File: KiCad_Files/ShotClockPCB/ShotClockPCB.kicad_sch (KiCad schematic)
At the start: 0 parts

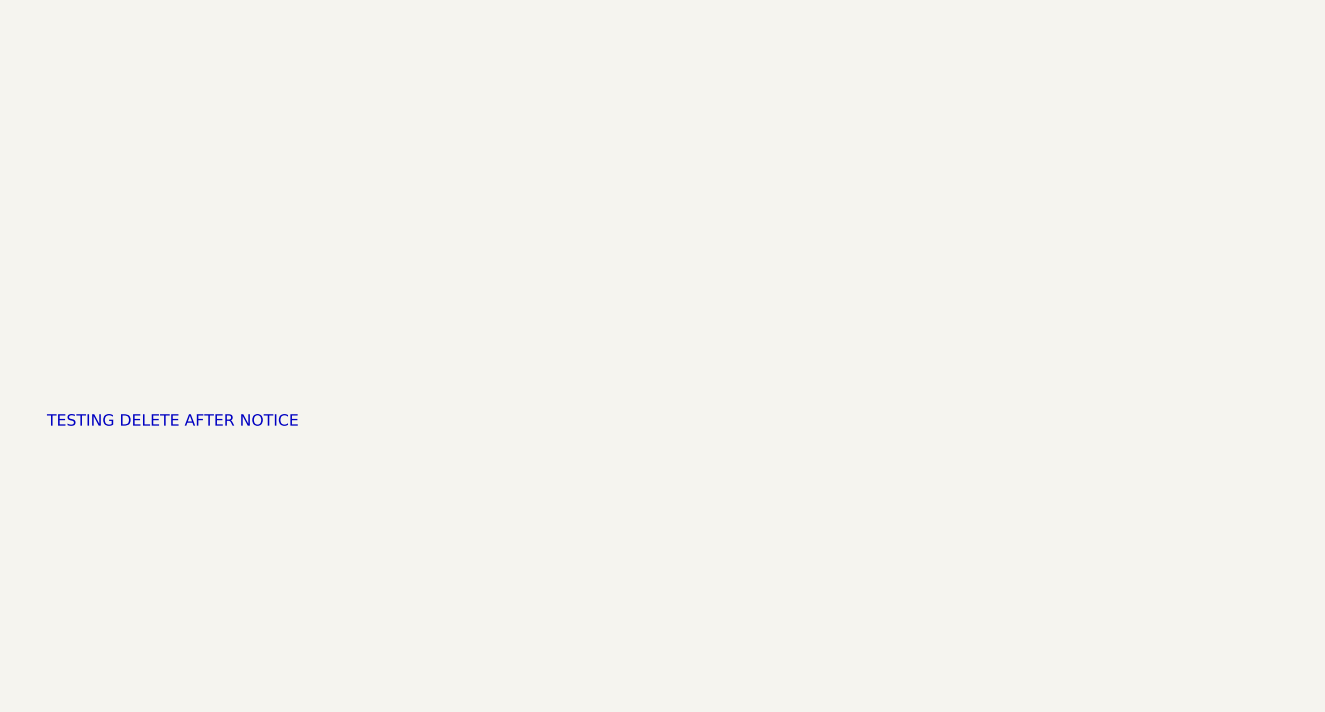
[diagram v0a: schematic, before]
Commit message: Added KiCad Schem and KiCad footprint libraries
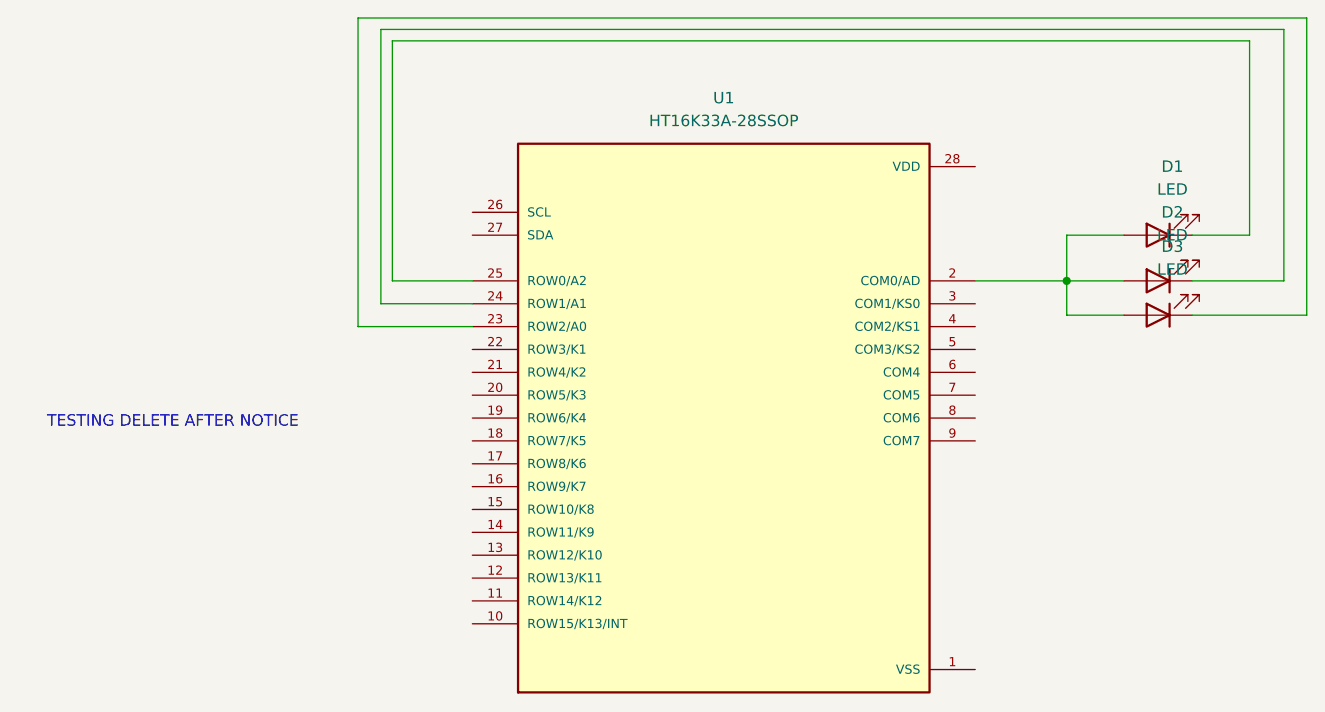
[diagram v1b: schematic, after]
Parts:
- added D1, D2, D3: LED, symbol Device:LED
- added U1: HT16K33A-28SSOP, HT16K33A-28SSOP:SOP63P600X175-28N, symbol HT16K33A-28SSOP:HT16K33A-28SSOP
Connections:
- new net: D1.2 (A), D2.2 (A), D3.2 (A), U1.2 (COM0/AD)
- new net: D3.1 (K), U1.23 (ROW2/A0)
- new net: D2.1 (K), U1.24 (ROW1/A1)
- new net: D1.1 (K), U1.25 (ROW0/A2)
